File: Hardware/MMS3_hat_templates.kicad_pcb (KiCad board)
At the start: 2 copper layers, 100 x 50 mm, 28 parts, among them J1 Chainbus in, J2 Chainbus Out, J3 Conn_01x04_Pin, J4 AMASS XT60 Male, J5 AMASS XT60 Female, U1 SN74CB3Q3384APW, U2 M24C64, U4 AMS1117

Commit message: removed tooling holes
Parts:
- removed H7, H8, H9: ~, PCM_JLCPCB:Hole_Tooling_JLCPCB
- R1: value 330Ω -> 10kΩ; footprint PCM_JLCPCB:R_0402 -> PCM_JLCPCB:R_0603
- R10, R4, R6: footprint PCM_JLCPCB:R_0402 -> PCM_JLCPCB:R_0603
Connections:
- R1 pad 1: /Bus_switch/SEL1 -> /Bus_switch/Chainbus.MOSI
- R1 pad 2: Net-(D3-Pad1) -> GND
- R4 pad 1: /Bus_switch/SEL1 -> +3V3
- R4 pad 2: +3V3 -> /Bus_switch/SEL1

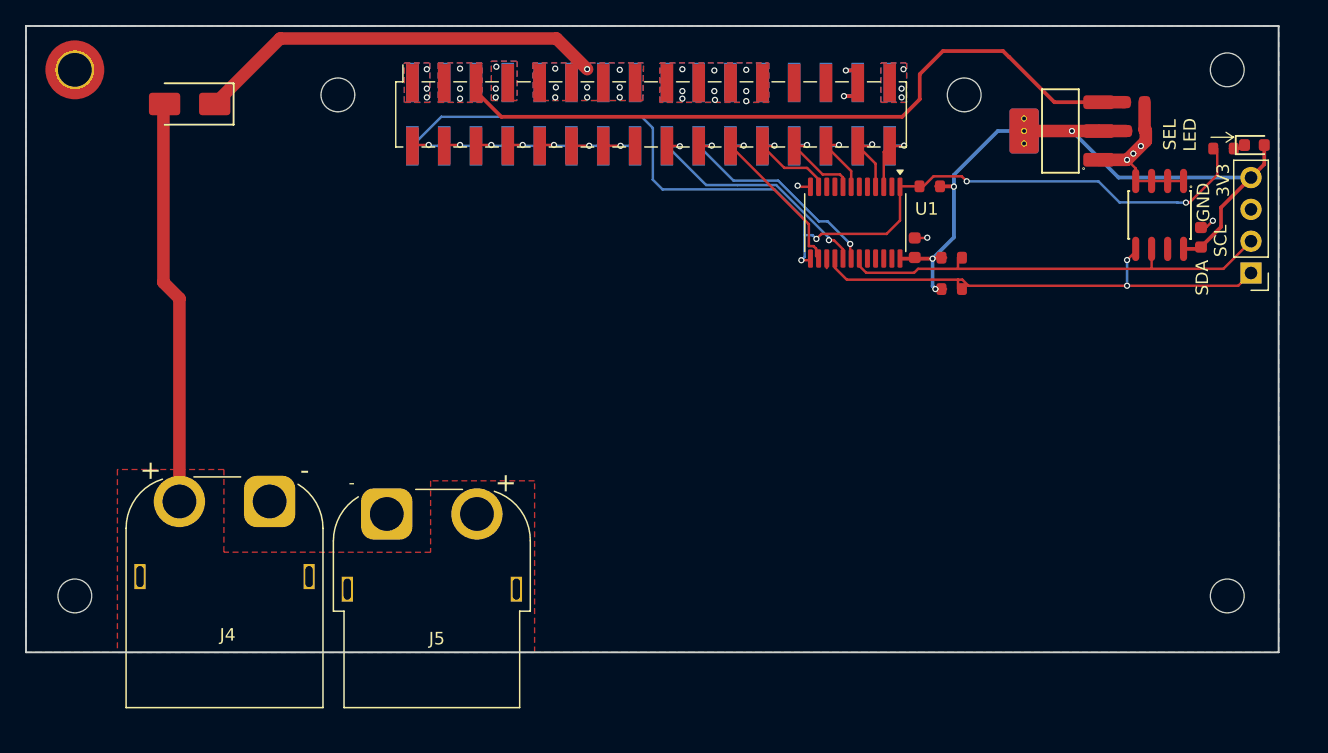
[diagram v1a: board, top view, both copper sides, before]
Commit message: changed numbering to per-sheet
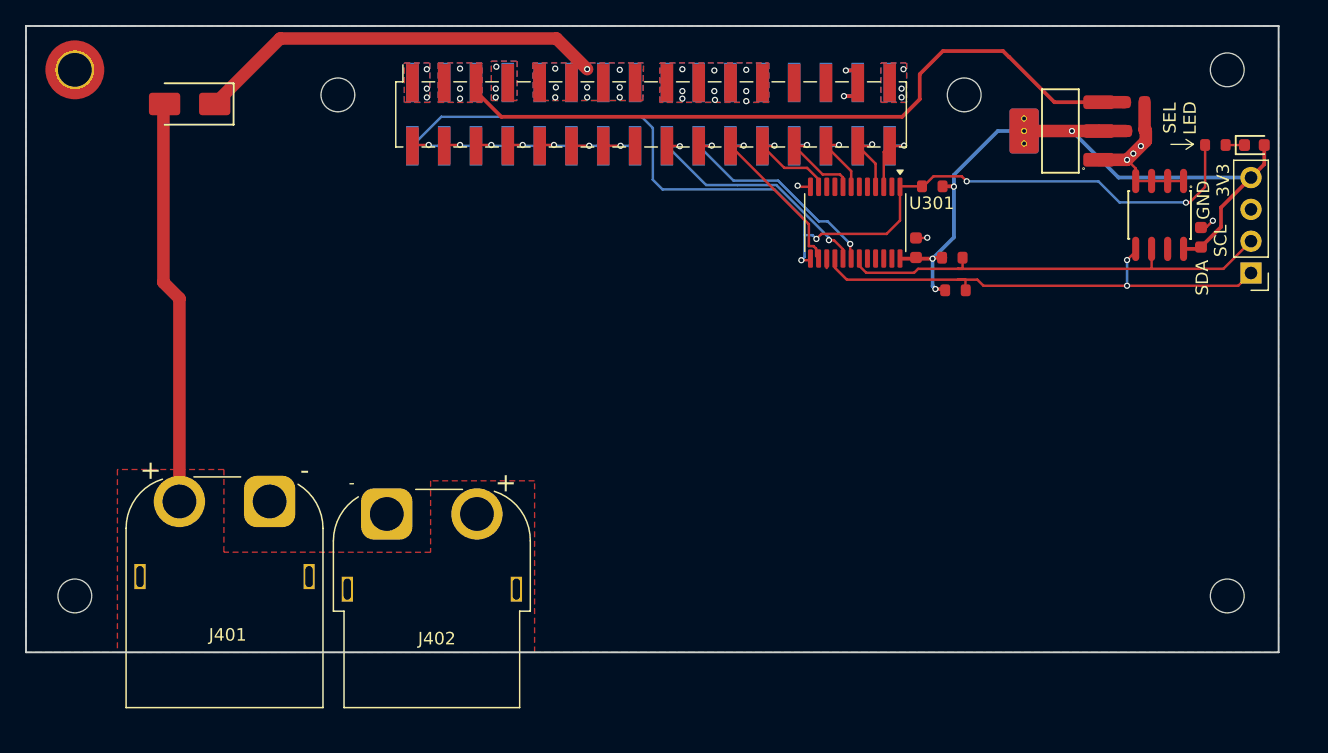
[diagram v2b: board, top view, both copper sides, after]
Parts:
- R311: renamed from R1; value 10kΩ -> 1kΩ
- moved R311 0.71 mm to (173.1, 98.0)
- moved R308 0.32 mm to (152.3, 109.6)
- moved R310 0.20 mm to (150.4, 101.3), turned to 180 degrees
- moved C301 0.10 mm to (149.2, 106.2)
- moved R304 0.05 mm to (152.1, 107.0)
- renumbered C16 to C101, C18 to C102, C1 to C301, C2 to C501, D3 to D301, D1 to D401, H1 to H101, H3 to H102, H2 to H103, H4 to H104, H6 to H105, H5 to H106, J1 to J201, J2 to J202, J3 to J301, J4 to J401, J5 to J402, R6 to R304, R10 to R308, R4 to R310, U4 to U101, U1 to U301, U2 to U501
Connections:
- D301 pad 1: Net-(D3-Pad1) -> Net-(D301-Pad1)
- R311 pad 1: /Bus_switch/Chainbus.MOSI -> /Bus_switch/SEL1
- R311 pad 2: GND -> Net-(D301-Pad1)
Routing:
- net Net-(D3-Pad1): track 1.57 -> 0.00 mm
- net Net-(D301-Pad1): track 0.00 -> 1.51 mm
- net /Bus_switch/Chainbus.SDA: track 38.9 -> 39.7 mm
- net +3V3: track 59.0 -> 58.5 mm

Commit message: moved elements to intiger value dimensions
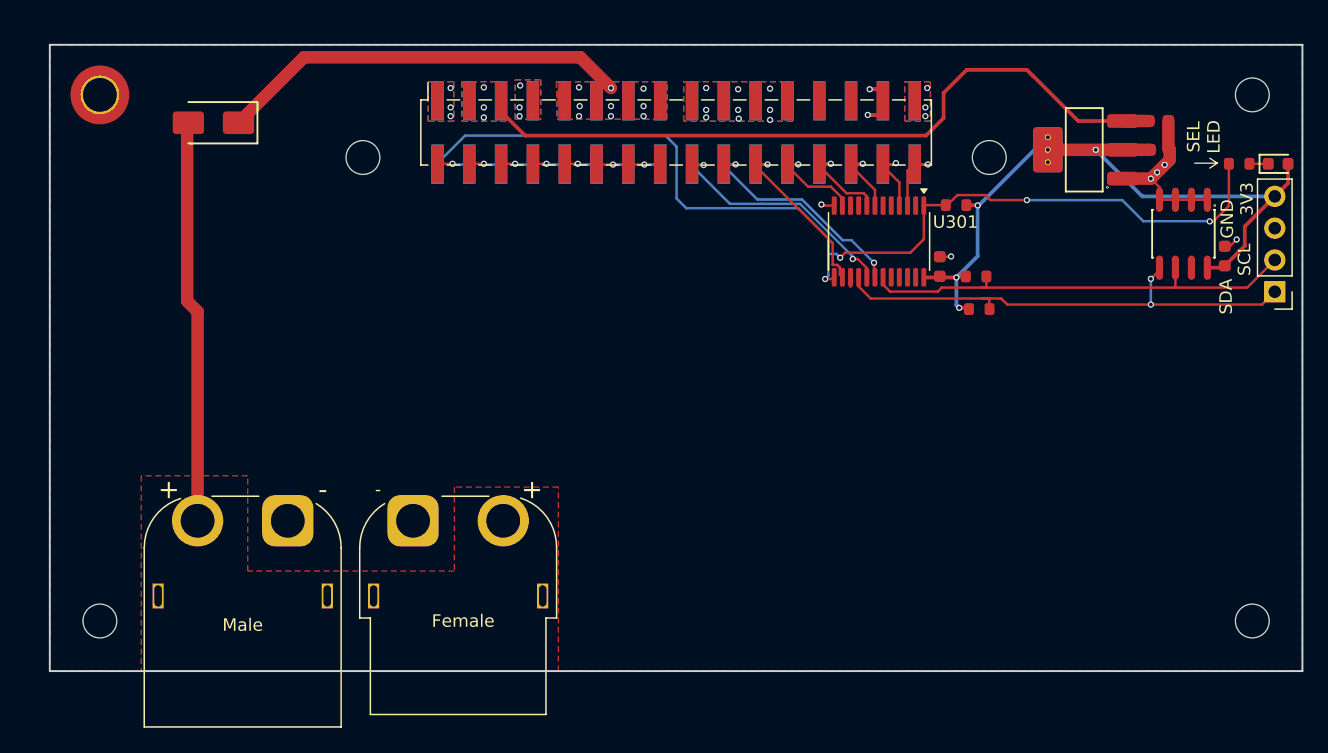
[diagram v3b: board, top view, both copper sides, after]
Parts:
- moved H105 5.39 mm to (155.0, 99.0)
- moved H106 5.39 mm to (105.0, 99.0)
- moved H101 2.83 mm to (84.0, 94.0)
- moved H102 2.83 mm to (84.0, 136.0)
- moved H103 2.83 mm to (176.0, 136.0)
- moved H104 2.83 mm to (176.0, 94.0)
- moved J201 2.49 mm to (130.0, 97.0)
- moved J202 2.47 mm to (130.0, 97.0)
- moved C101 2.42 mm to (168.5, 96.1)
- moved C102 2.42 mm to (168.6, 98.4)
- moved C301 2.42 mm to (151.1, 107.7)
- moved C501 2.42 mm to (173.8, 106.9)
- moved D301 2.42 mm to (178.1, 99.5)
- moved G*** 2.42 mm to (167.8, 129.2)
- moved R310 2.42 mm to (152.3, 102.8)
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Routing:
- net +3V3: track 58.5 -> 57.9 mm
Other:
- board text added: "Female"
- board text added: "Male"

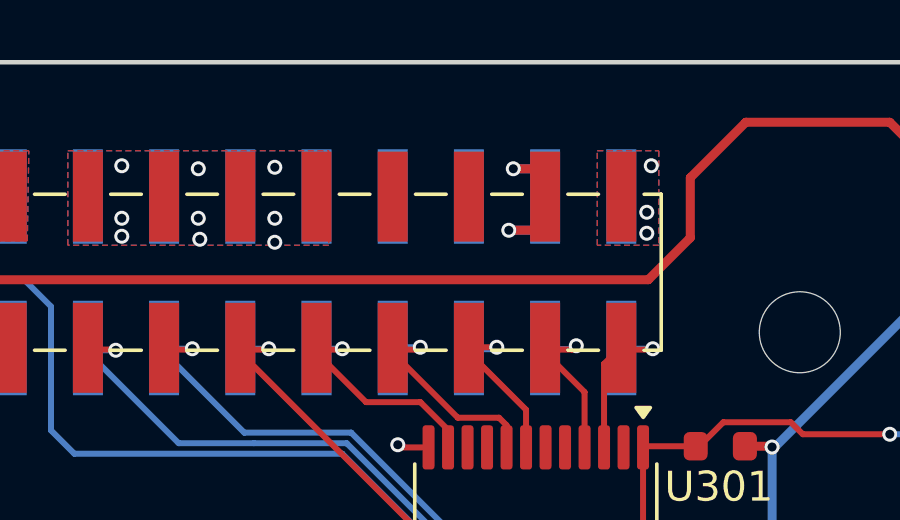
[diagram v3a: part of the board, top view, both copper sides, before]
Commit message: MAJOR CHANGE - Pins 25 27 of chainbus connected
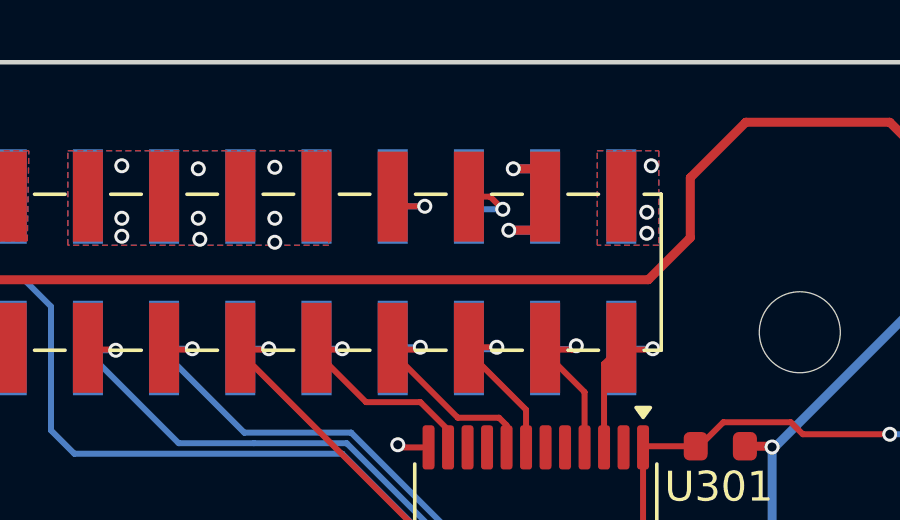
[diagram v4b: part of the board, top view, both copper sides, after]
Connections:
- J201 pad 25: unconnected-(J201-Pin_25-Pad25) -> /Interboard_connector/Pin_25
- J201 pad 27: unconnected-(J201-Pin_27-Pad27) -> /Interboard_connector/Pin_27
- J202 pad 25: unconnected-(J202-Pin_25-Pad25) -> /Interboard_connector/Pin_25
- J202 pad 27: unconnected-(J202-Pin_27-Pad27) -> /Interboard_connector/Pin_27
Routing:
- net /Interboard_connector/Pin_27: track 0.00 -> 2.61 mm, vias 0 -> 1
- net /Interboard_connector/Pin_25: track 0.00 -> 2.41 mm, vias 0 -> 1
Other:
- board text added: "Front and Back keepout zone for mounting"
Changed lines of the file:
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@@
 			(size 3 1)
 			(layers "F.Cu" "F.Mask" "F.Paste")
-			(net "unconnected-(J202-Pin_25-Pad25)")
+			(net "/Interboard_connector/Pin_25")
 			(pinfunction "Pin_25_25")
-			(pintype "passive+no_connect")
+			(pintype "passive")
 		)
 		(pad "26" smd rect
@@
 			(size 3 1)
 			(layers "F.Cu" "F.Mask" "F.Paste")
-			(net "unconnected-(J202-Pin_27-Pad27)")
+			(net "/Interboard_connector/Pin_27")
 			(pinfunction "Pin_27_27")
-			(pintype "passive+no_connect")
+			(pintype "passive")
 		)
 		(pad "28" smd rect
@@
 			(size 3.15 1)
 			(layers "B.Cu" "B.Mask" "B.Paste")
-			(net "unconnected-(J201-Pin_25-Pad25)")
+			(net "/Interboard_connector/Pin_25")
 			(pinfunction "Pin_25_25")
-			(pintype "passive+no_connect")
+			(pintype "passive")
 		)
 		(pad "26" smd rect
@@
 			(size 3.15 1)
 			(layers "B.Cu" "B.Mask" "B.Paste")
-			(net "unconnected-(J201-Pin_27-Pad27)")
+			(net "/Interboard_connector/Pin_27")
 			(pinfunction "Pin_27_27")
-			(pintype "passive+no_connect")
+			(pintype "passive")
 		)
 		(pad "28" smd rect
@@
 		(end 87 140)
 		(stroke
-			(width 0.1)
-			(type default)
+			(width 0.3)
+			(type solid)
 		)
 		(fill no)
@@
 		(end 180 140)
 		(stroke
-			(width 0.1)
-			(type default)
+			(width 0.3)
+			(type solid)
 		)
 		(fill no)
@@
 	)
 	(gr_line
+		(start 182 135)
+		(end 182 131)
+		(stroke
+			(width 0.5)
+			(type solid)
+		)
+		(layer "Eco1.User")
+	)
+	(gr_line
 		(start 182.1 88)
 		(end 182.1 84)
@@
 	)
 	(gr_line
+		(start 186 135)
+		(end 182 135)
+		(stroke
+			(width 0.5)
+			(type solid)
+		)
+		(layer "Eco1.User")
+	)
+	(gr_line
 		(start 186.1 88)
 		(end 182.1 88)
@@
 	)
 	(gr_line
+		(start 188 130)
+		(end 182 135)
+		(stroke
+			(width 0.5)
+			(type solid)
+		)
+		(layer "Eco1.User")
+	)
+	(gr_line
 		(start 188.1 83)
 		(end 182.1 88)
@@
 		)
 	)
+	(gr_text "Front and Back keepout\nzone for mounting"
+		(at 184 128 0)
+		(layer "Eco1.User")
+		(effects
+			(font
+				(size 1 1)
+				(thickness 0.2)
+				(bold yes)
+			)
+			(justify left bottom)
+		)
+	)
 	(gr_text "Front and Back keepout\nzone for DIN rail mount"
 		(at 184.1 81 0)
@@
 		(net "Net-(D301-Pad1)")
 	)
+	(segment
+		(start 141.58 94.48)
+		(end 141.43 94.48)
+		(width 0.2)
+		(layer "F.Cu")
+		(net "/Interboard_connector/Pin_25")
+	)
+	(segment
+		(start 142.5 94.8)
+		(end 141.9 94.8)
+		(width 0.2)
+		(layer "F.Cu")
+		(net "/Interboard_connector/Pin_25")
+	)
+	(segment
+		(start 141.9 94.8)
+		(end 141.58 94.48)
+		(width 0.2)
+		(layer "F.Cu")
+		(net "/Interboard_connector/Pin_25")
+	)
+	(via
+		(at 142.5 94.8)
+		(size 0.5)
+		(drill 0.3)
+		(layers "F.Cu" "B.Cu")
+		(net "/Interboard_connector/Pin_25")
+	)
+	(segment
+		(start 142.5 94.8)
+		(end 141.755 94.8)
+		(width 0.2)
+		(layer "B.Cu")
+		(net "/Interboard_connector/Pin_25")
+	)
+	(segment
+		(start 141.755 94.8)
+		(end 141.43 94.475)
+		(width 0.2)
+		(layer "B.Cu")
+		(net "/Interboard_connector/Pin_25")
+	)
+	(segment
+		(start 144.68 94.48)
+		(end 145.1 94.9)
+		(width 0.2)
+		(layer "F.Cu")
+		(net "/Interboard_connector/Pin_27")
+	)
+	(segment
+		(start 143.97 94.48)
+		(end 144.68 94.48)
+		(width 0.2)
+		(layer "F.Cu")
+		(net "/Interboard_connector/Pin_27")
+	)
+	(via
+		(at 145.1 94.9)
+		(size 0.5)
+		(drill 0.3)
+		(layers "F.Cu" "B.Cu")
+		(net "/Interboard_connector/Pin_27")
+	)
+	(segment
+		(start 144.395 94.9)
+		(end 143.97 94.475)
+		(width 0.2)
+		(layer "B.Cu")
+		(net "/Interboard_connector/Pin_27")
+	)
+	(segment
+		(start 145.1 94.9)
+		(end 144.395 94.9)
+		(width 0.2)
+		(layer "B.Cu")
+		(net "/Interboard_connector/Pin_27")
+	)
 	(zone

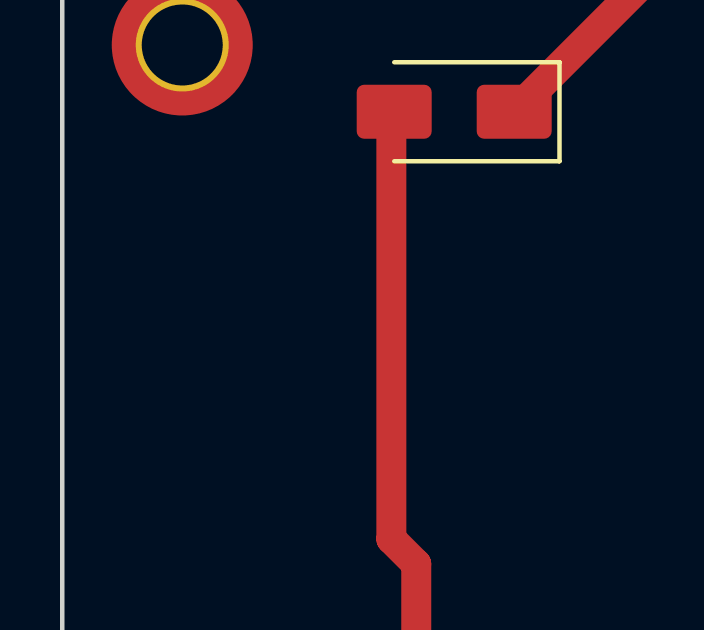
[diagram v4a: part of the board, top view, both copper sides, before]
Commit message: added nameplate to template
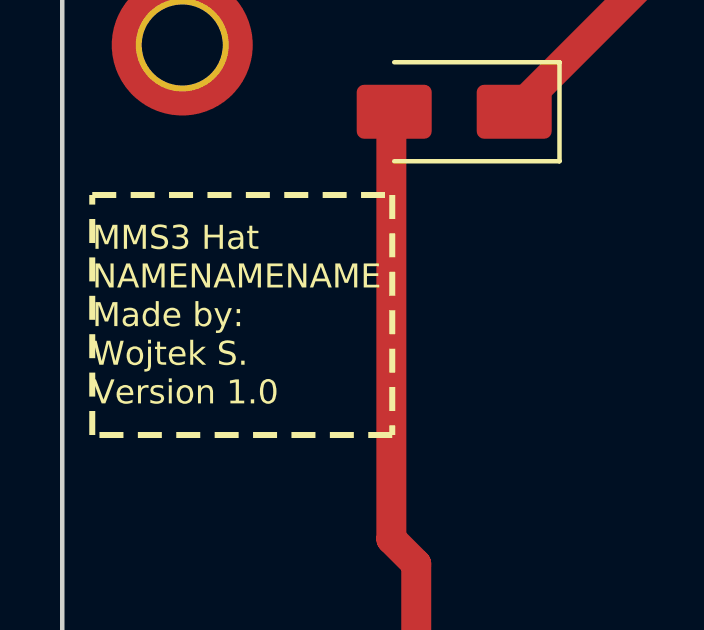
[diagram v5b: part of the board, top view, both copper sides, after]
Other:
- board text added: "MMS3 Hat NAMENAMENAME Made by: Wojtek S. Version 1.0"
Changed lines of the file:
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@@
 		(embedded_fonts no)
 	)
+	(gr_rect
+		(start 81 99)
+		(end 91 107)
+		(stroke
+			(width 0.2)
+			(type dash)
+		)
+		(fill no)
+		(layer "F.SilkS")
+	)
 	(gr_line
 		(start 173.2 99.45)
@@
 		(layer "Edge.Cuts")
 	)
+	(gr_text "MMS3 Hat\nNAMENAMENAME\nMade by:\nWojtek S.\nVersion 1.0"
+		(at 81 103 0)
+		(layer "F.SilkS")
+		(effects
+			(font
+				(size 0.8 0.8)
+				(thickness 0.1)
+			)
+			(justify left)
+		)
+	)
 	(gr_text "Male"
 		(at 95.4 136.320647 0)
@@
 	)
 	(segment
+		(start 141.58 94.48)
+		(end 141.43 94.48)
+		(width 0.2)
+		(layer "F.Cu")
+		(net "/Interboard_connector/Pin_25")
+	)
+	(segment
+		(start 142.5 94.8)
+		(end 141.9 94.8)
+		(width 0.2)
+		(layer "F.Cu")
+		(net "/Interboard_connector/Pin_25")
+	)
+	(segment
+		(start 141.9 94.8)
+		(end 141.58 94.48)
+		(width 0.2)
+		(layer "F.Cu")
+		(net "/Interboard_connector/Pin_25")
+	)
+	(via
+		(at 142.5 94.8)
+		(size 0.5)
+		(drill 0.3)
+		(layers "F.Cu" "B.Cu")
+		(net "/Interboard_connector/Pin_25")
+	)
+	(segment
+		(start 142.5 94.8)
+		(end 141.755 94.8)
+		(width 0.2)
+		(layer "B.Cu")
+		(net "/Interboard_connector/Pin_25")
+	)
+	(segment
+		(start 141.755 94.8)
+		(end 141.43 94.475)
+		(width 0.2)
+		(layer "B.Cu")
+		(net "/Interboard_connector/Pin_25")
+	)
+	(segment
+		(start 144.68 94.48)
+		(end 145.1 94.9)
+		(width 0.2)
+		(layer "F.Cu")
+		(net "/Interboard_connector/Pin_27")
+	)
+	(segment
+		(start 143.97 94.48)
+		(end 144.68 94.48)
+		(width 0.2)
+		(layer "F.Cu")
+		(net "/Interboard_connector/Pin_27")
+	)
+	(via
+		(at 145.1 94.9)
+		(size 0.5)
+		(drill 0.3)
+		(layers "F.Cu" "B.Cu")
+		(net "/Interboard_connector/Pin_27")
+	)
+	(segment
+		(start 144.395 94.9)
+		(end 143.97 94.475)
+		(width 0.2)
+		(layer "B.Cu")
+		(net "/Interboard_connector/Pin_27")
+	)
+	(segment
+		(start 145.1 94.9)
+		(end 144.395 94.9)
+		(width 0.2)
+		(layer "B.Cu")
+		(net "/Interboard_connector/Pin_27")
+	)
+	(segment
 		(start 145.4 93.55)
 		(end 146.4 93.55)
@@
 		(net "Net-(D301-Pad1)")
 	)
-	(segment
-		(start 141.58 94.48)
-		(end 141.43 94.48)
-		(width 0.2)
-		(layer "F.Cu")
-		(net "/Interboard_connector/Pin_25")
-	)
-	(segment
-		(start 142.5 94.8)
-		(end 141.9 94.8)
-		(width 0.2)
-		(layer "F.Cu")
-		(net "/Interboard_connector/Pin_25")
-	)
-	(segment
-		(start 141.9 94.8)
-		(end 141.58 94.48)
-		(width 0.2)
-		(layer "F.Cu")
-		(net "/Interboard_connector/Pin_25")
-	)
-	(via
-		(at 142.5 94.8)
-		(size 0.5)
-		(drill 0.3)
-		(layers "F.Cu" "B.Cu")
-		(net "/Interboard_connector/Pin_25")
-	)
-	(segment
-		(start 142.5 94.8)
-		(end 141.755 94.8)
-		(width 0.2)
-		(layer "B.Cu")
-		(net "/Interboard_connector/Pin_25")
-	)
-	(segment
-		(start 141.755 94.8)
-		(end 141.43 94.475)
-		(width 0.2)
-		(layer "B.Cu")
-		(net "/Interboard_connector/Pin_25")
-	)
-	(segment
-		(start 144.68 94.48)
-		(end 145.1 94.9)
-		(width 0.2)
-		(layer "F.Cu")
-		(net "/Interboard_connector/Pin_27")
-	)
-	(segment
-		(start 143.97 94.48)
-		(end 144.68 94.48)
-		(width 0.2)
-		(layer "F.Cu")
-		(net "/Interboard_connector/Pin_27")
-	)
-	(via
-		(at 145.1 94.9)
-		(size 0.5)
-		(drill 0.3)
-		(layers "F.Cu" "B.Cu")
-		(net "/Interboard_connector/Pin_27")
-	)
-	(segment
-		(start 144.395 94.9)
-		(end 143.97 94.475)
-		(width 0.2)
-		(layer "B.Cu")
-		(net "/Interboard_connector/Pin_27")
-	)
-	(segment
-		(start 145.1 94.9)
-		(end 144.395 94.9)
-		(width 0.2)
-		(layer "B.Cu")
-		(net "/Interboard_connector/Pin_27")
-	)
 	(zone
